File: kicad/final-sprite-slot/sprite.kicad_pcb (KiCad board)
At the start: 4 copper layers, 35 x 44.6 mm, 66 parts, among them J1 M20-7910442R, U1 CC430F513X, U2 LSM9DS1, U3 SPRITETCXO_TCXO_7Z, U4 DRV8837, U5 ADP5092, U6 DRV8837, U7 DRV8837, X1 SPRITEPIN_SPRITE_PIN, X2 SPRITEPIN_SPRITE_PIN

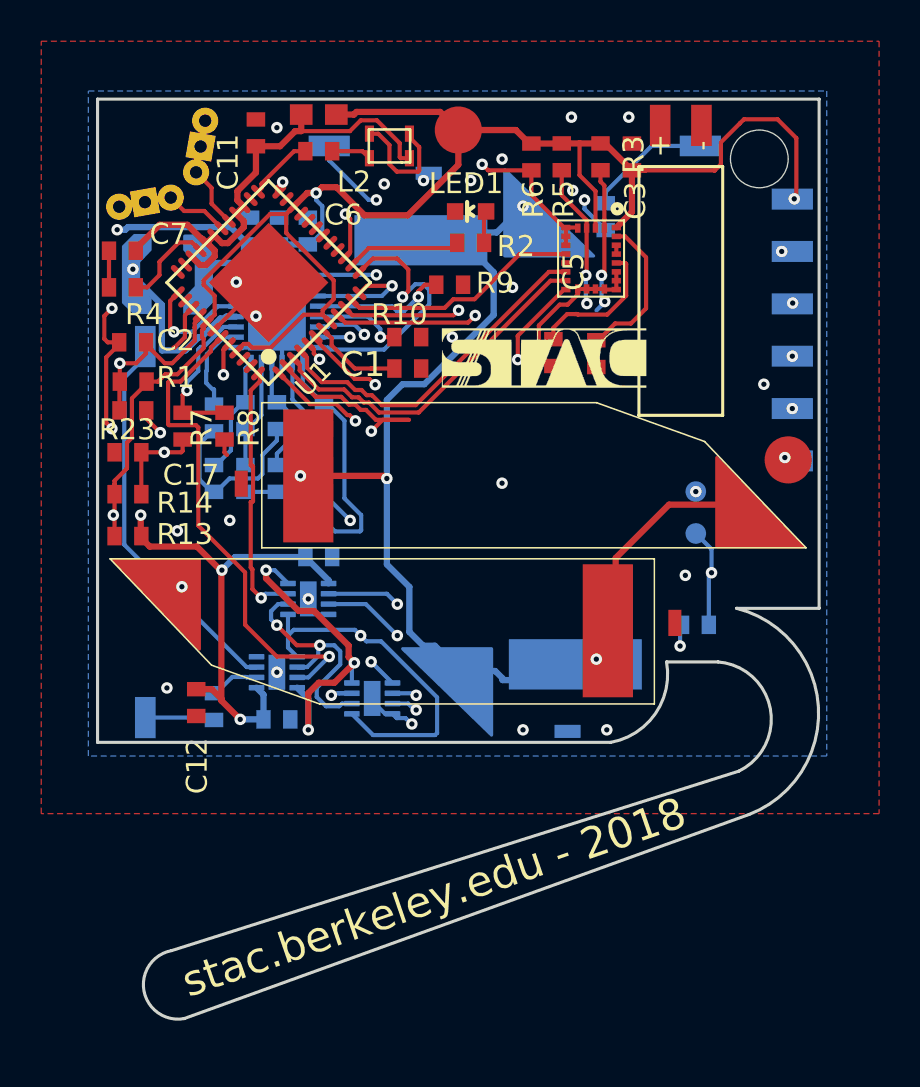
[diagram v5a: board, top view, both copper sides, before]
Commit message: Added edge cut. Final version probably
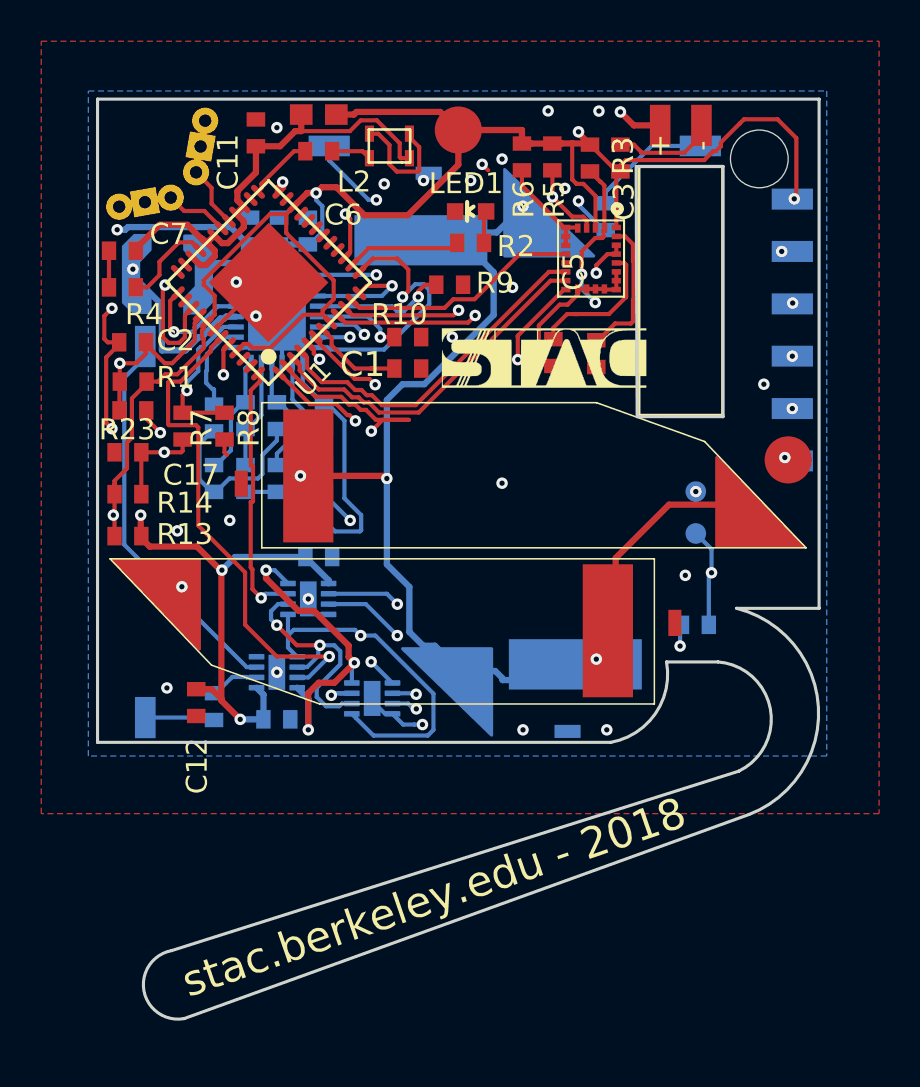
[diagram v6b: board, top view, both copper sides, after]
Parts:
- moved C3 0.56 mm to (146.2, 86.3)
- moved R3 0.51 mm to (144.7, 86.3)
- moved R5 0.46 mm to (142.9, 86.3)
- moved R6 0.46 mm to (141.4, 86.3)
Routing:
- net Net-(R22-Pad1): track 555.1 -> 432.3 mm
- net /UART_TX: track 1.08 -> 51.7 mm
- net /TST: track 2.41 -> 50.7 mm, vias 1 -> 2
- net /UART_RX: track 4.06 -> 43.0 mm
- net /VBAT: track 4.76 -> 22.3 mm, vias 1 -> 2
- net VCC: track 132.1 -> 141.3 mm, vias 6 -> 8
- net /~RST: track 51.2 -> 57.1 mm
- net GND: track 45.9 -> 51.3 mm
- net /SDA: track 19.5 -> 17.4 mm, vias 3 -> 2
- net Net-(R6-Pad2): track 28.3 -> 26.4 mm
- net Net-(C5-Pad1): track 7.39 -> 6.89 mm
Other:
- outline, holes or cut-outs redrawn
